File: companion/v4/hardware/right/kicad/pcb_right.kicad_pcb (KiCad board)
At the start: 2 copper layers, 44.5 x 19 mm, 55 parts, among them J1 TF31-6S-0.5SH_800_, J2 speaker, J3 USB_C_Receptacle_USB2.0_14P, J4 Conn_01x24_MountingPin, SW1 SW_BOOT, SW3 SW_RESET, U2 MAX98357AETE_T, U3 USBLC6-2SC6, U4 ESP32-S3-MINI-1, U5 TLV75528PDBV, U6 TPS63001, U7 TLV75515PDBV

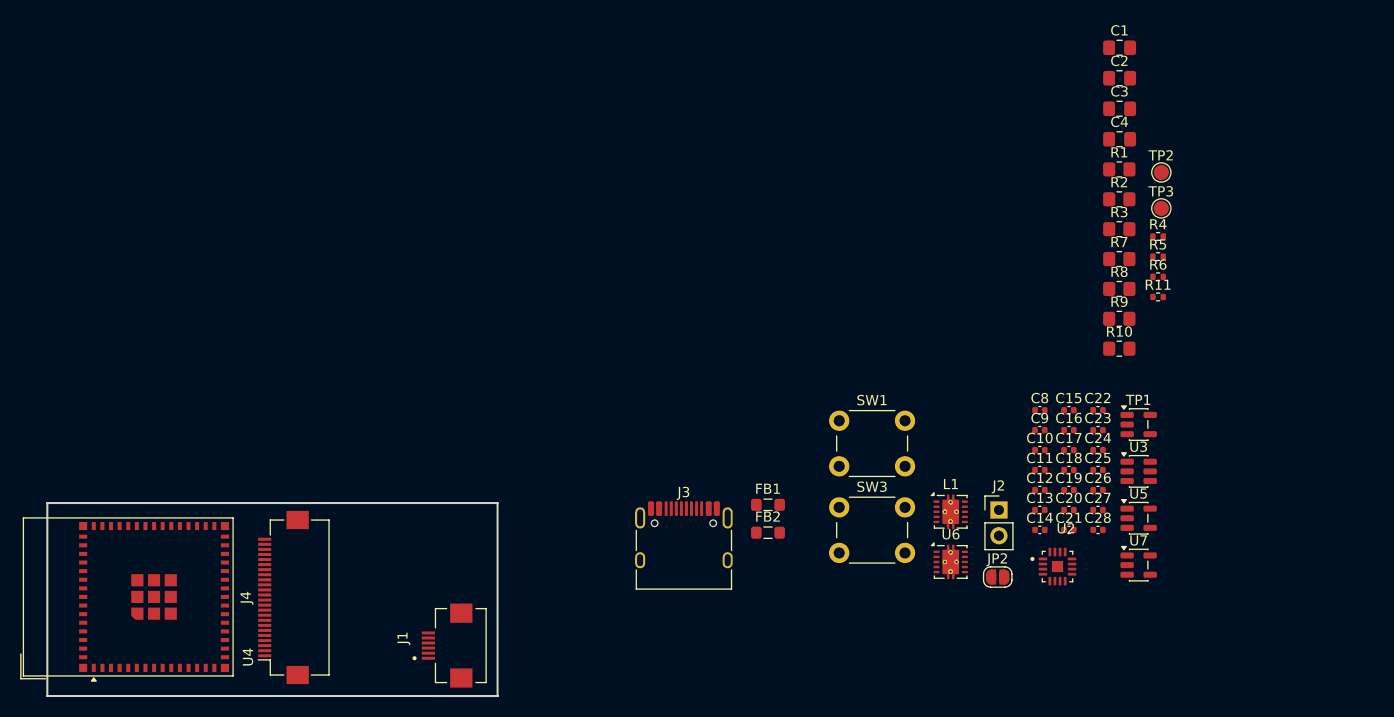
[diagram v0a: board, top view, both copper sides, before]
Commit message: Complete right PCB rev 1 layout and BOM
Finish rev 1 layout for the v4 right board, add fabrication outputs
(BOM, positions, netlist, gerbers), shared Master_lib symbols and
footprints, 3D models, and PCB renders.

Co-Authored-By: Claude Opus 5.5 <noreply@anthropic.com>
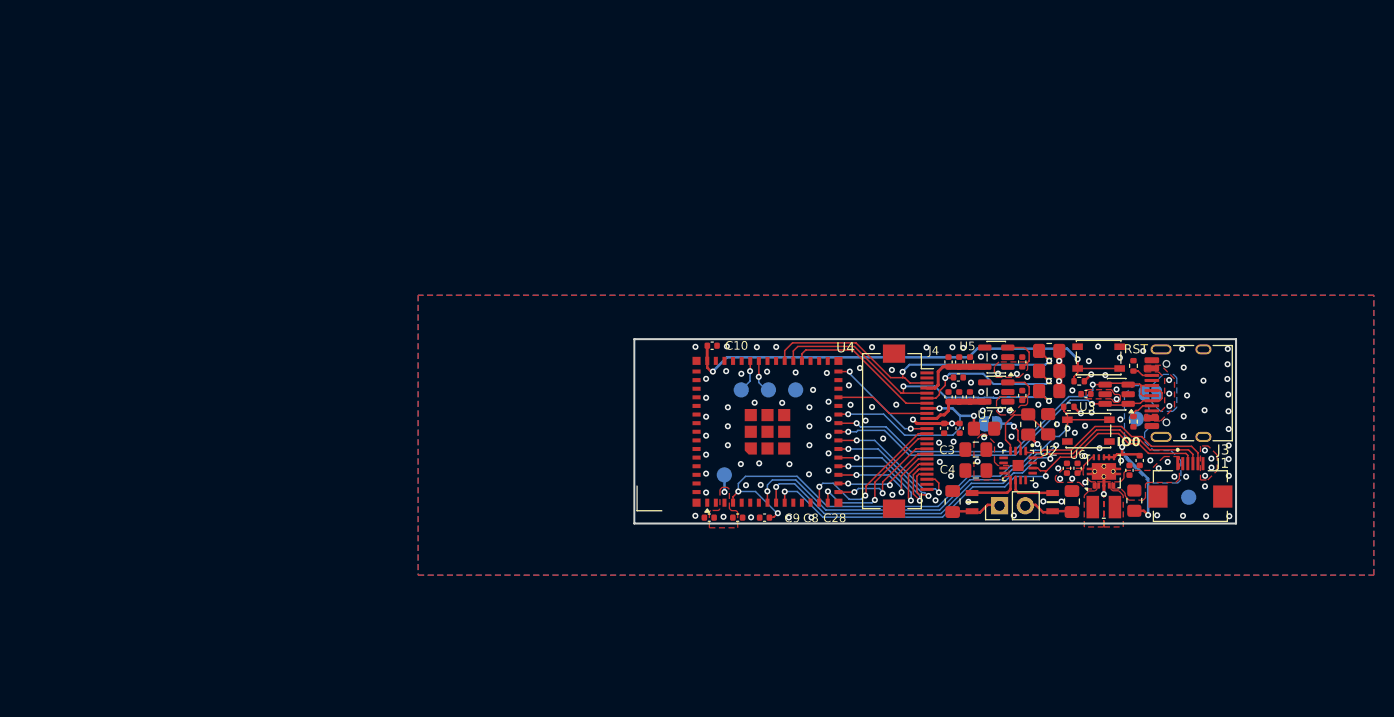
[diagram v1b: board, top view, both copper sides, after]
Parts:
- removed C23: 47uf, Capacitor_SMD:C_0402_1005Metric
- added JP3: SolderJumper_2_Open, Jumper:SolderJumper-2_P1.3mm_Open_RoundedPad1.0x1.5mm, B.Cu at (172.4, 97.1)
- added TP4: GND, TestPoint:TestPoint_Pad_D1.5mm, B.Cu at (130.3, 105.2)
- added TP5: GND, TestPoint:TestPoint_Pad_D1.5mm, B.Cu at (171.0, 99.7)
- added TP6: GND, TestPoint:TestPoint_Pad_D1.5mm, B.Cu at (176.2, 107.4)
- C1, C2: value 220PF -> 220pF
- C10: value 1u -> 1uF
- C11, C12, C14, C15, C17, C19, C21: value 1uf -> 1uF
- C13, C16: value 100n -> 0.1uF
- C18, C20, C22: value 100nf -> 0.1uF
- C24, C26, C27, C8: value 10uf -> 10uF
- C25, C28, C9: value 0.1uf -> 0.1uF
- C3: value 0.1UF -> 0.1uF
- C4: value 10UF -> 10uF
- FB1, FB2: value FerriteBead -> BLM21PG600SN1D; footprint Inductor_SMD:L_0805_2012Metric_Pad1.05x1.20mm_HandSolder -> Master_lib:BLM21AG102BH1J
- J1: footprint HRS_TF31-6S-0.5SH_800_:HRS_TF31-6S-0.5SH_800_ -> Master_lib:HRS_TF31-6S-0.5SH_800_
- J3: footprint Connector_USB:USB_C_Receptacle_HRO_TYPE-C-31-M-12 -> Master_lib:USB_C_Receptacle_HRO_TYPE-C-31-M-12
- JP2, TP2, TP3: moved to B.Cu
- L1: footprint Package_SON:Texas_DRC0010J_ThermalVias -> Master_lib:INDC2520X120N
- R1, R2: value 100k -> 100K
- R10, R9: value 10k -> 10K
- R11, R4: value 10kΩ -> 10K
- R3: value 100 -> 100R
- R5, R6: value 5.1kΩ -> 5.1K
- R7, R8: value 4.7k -> 4.7K
- SW1, SW3: footprint Button_Switch_THT:SW_PUSH_6mm_H5mm -> Button_Switch_SMD:SW_SPST_PTS810
- TP1: footprint Package_TO_SOT_SMD:SOT-23-5 -> TestPoint:TestPoint_Pad_D1.5mm; moved to B.Cu
- U2: footprint MAX98357A:QFN50P300X300X80-17N -> Master_lib:QFN50P300X300X80-17N
- U4: footprint RF_Module:ESP32-S2-MINI-1 -> Master_lib:ESP32-S2-MINI-1
- U6: footprint Package_SON:Texas_DRC0010J_ThermalVias -> Master_lib:Texas_DRC0010J_ThermalVias
- moved J1 73.5 mm to (176.3, 107.3), turned to 180 degrees
- moved J4 63.8 mm to (148.5, 100.8), turned to -90 degrees
- moved U4 62.7 mm to (132.0, 100.9)
- moved J3 52.6 mm to (176.6, 97.1), turned to 90 degrees
- moved C1 47.7 mm to (152.9, 107.8), turned to 90 degrees
- moved TP2 46.7 mm to (132.0, 96.8), turned to 90 degrees
- moved C2 42.0 mm to (164.7, 107.8), turned to -90 degrees
- moved TP3 40.3 mm to (137.4, 96.8), turned to 90 degrees
- moved TP1 36.7 mm to (134.7, 96.8), turned to 90 degrees
- moved C3 36.5 mm to (155.2, 102.7), turned to 180 degrees
- moved C4 35.6 mm to (155.2, 104.7), turned to 180 degrees
- moved C10 34.0 mm to (129.1, 92.4)
- moved C9 33.8 mm to (128.8, 109.4), turned to 180 degrees
- moved C28 32.9 mm to (134.3, 109.4), turned to 180 degrees
- moved C8 31.7 mm to (131.7, 109.4)
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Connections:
- J3 pad A4: unconnected-(J3-VBUS-PadA4)_3 -> Net-(JP3-A)
- J3 pad A9: unconnected-(J3-VBUS-PadA4)_1 -> Net-(JP3-A)
- J3 pad B4: unconnected-(J3-VBUS-PadA4)_2 -> Net-(JP3-A)
- J3 pad B9: unconnected-(J3-VBUS-PadA4) -> Net-(JP3-A)
- U2 pad 12: (no net) -> unconnected-(U2-NC-Pad12)
- U2 pad 13: (no net) -> unconnected-(U2-NC-Pad13)
- U2 pad 5: (no net) -> unconnected-(U2-NC-Pad5)
- U2 pad 6: (no net) -> unconnected-(U2-NC-Pad6)
- U3 pad 1: USB_DP -> USB_DN
- U3 pad 3: USB_DN -> USB_DP
- U3 pad 4: USB_DN -> USB_DP
- U3 pad 6: USB_DP -> USB_DN
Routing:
- net DIN: track 0.00 -> 55.0 mm, vias 0 -> 2
- net BCLK: track 0.00 -> 51.7 mm, vias 0 -> 2
- net Net-(U4-IO0): track 0.00 -> 51.7 mm, vias 0 -> 3
- net LRCLK: track 0.00 -> 49.2 mm, vias 0 -> 2
- net Net-(U4-EN): track 0.00 -> 46.7 mm, vias 0 -> 2
- net USB_DN: track 0.00 -> 37.4 mm, vias 0 -> 2
- net USB_DP: track 0.00 -> 37.1 mm, vias 0 -> 2
- net CAM_SIOD: track 0.00 -> 34.0 mm, vias 0 -> 2
- net CAM_SIOC: track 0.00 -> 33.6 mm, vias 0 -> 2
- net +3.3V: track 0.00 -> 24.3 mm, vias 0 -> 23
- net CAM_PWDN: track 0.00 -> 20.5 mm, vias 0 -> 3
- net CAM_XCLK: track 0.00 -> 16.2 mm, vias 0 -> 2
- net CAM_RESET: track 0.00 -> 16.2 mm, vias 0 -> 2
- net CAM_VSYNC: track 0.00 -> 15.4 mm
- net CAM_Y8: track 0.00 -> 15.0 mm, vias 0 -> 2
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- added copper zone on F.Cu, net +3.3V
- added copper zone on In2.Cu, net +3.3V
- added copper zone on B.Cu, net +5V
- added copper zone on F.Cu, net +5V
- added copper zone on B.Cu, net GND
- added copper zone on F.Cu, net GND
- added copper zone on In1.Cu, net GND
- added copper zone on B.Cu, net Net-(JP3-A)
- added copper zone on F.Cu, net Net-(JP3-A)
- added copper zone on F.Cu, net Net-(U6-L1)
- added copper zone on F.Cu, net Net-(U6-L2)
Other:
- board size 44.5 x 19 mm -> 59.4 x 18.2 mm
- copper layers 2 -> 4
- board text added: "3V3"
- board text added: "5V"
- board text added: "GAIN"
- board text added: "GND"
- board text added: "IO0"
- board text added: "RST"
- board text added: "RXD0"
- board text added: "TXD0"
- board text added: "VBUS"
